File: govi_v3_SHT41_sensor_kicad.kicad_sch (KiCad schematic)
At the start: 5 parts

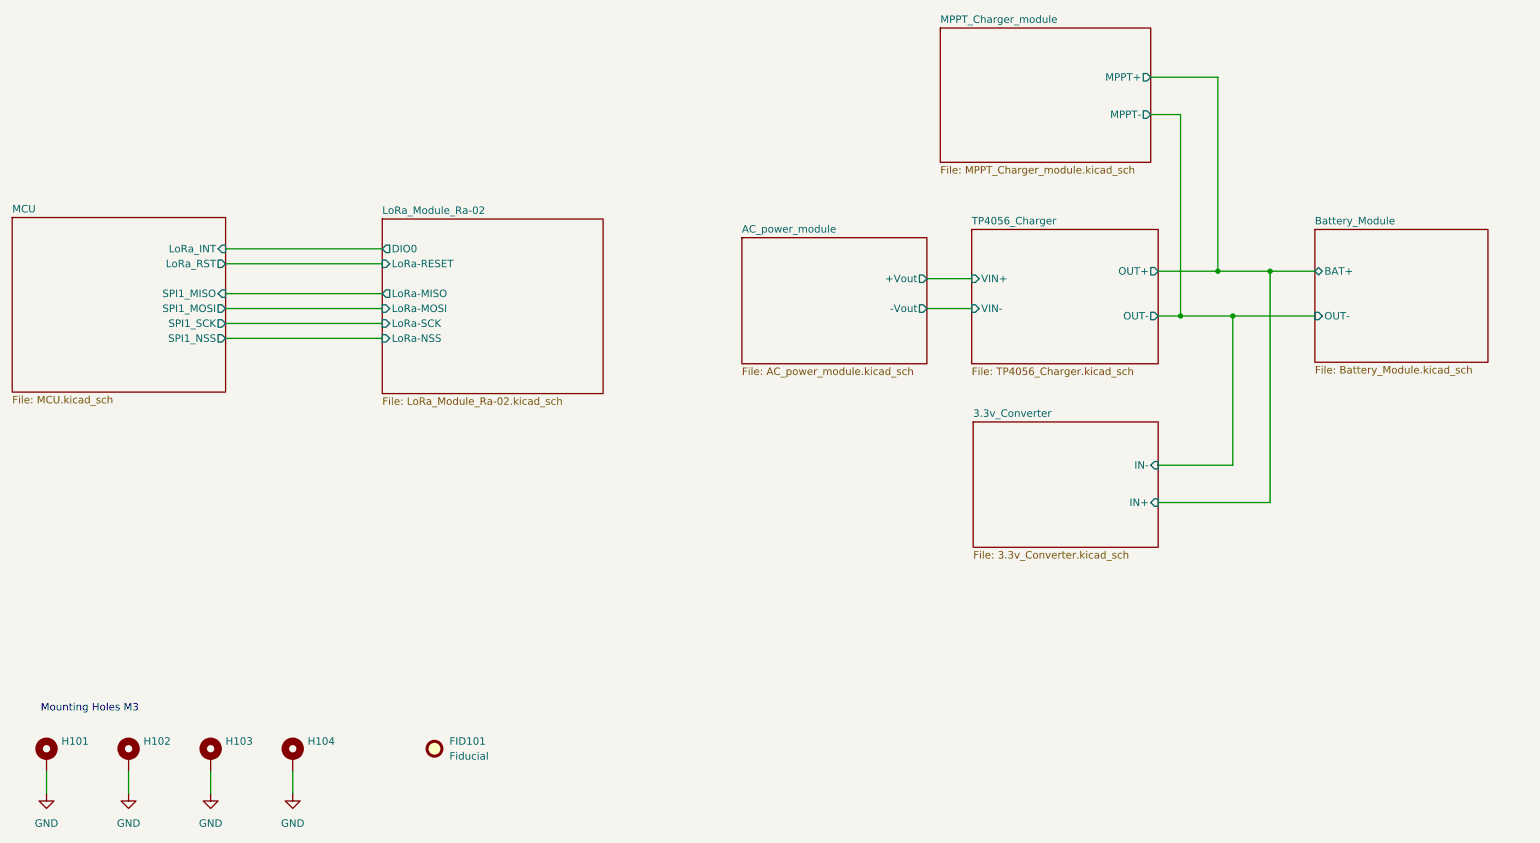
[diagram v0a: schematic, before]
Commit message: "Assign Footprints Done"
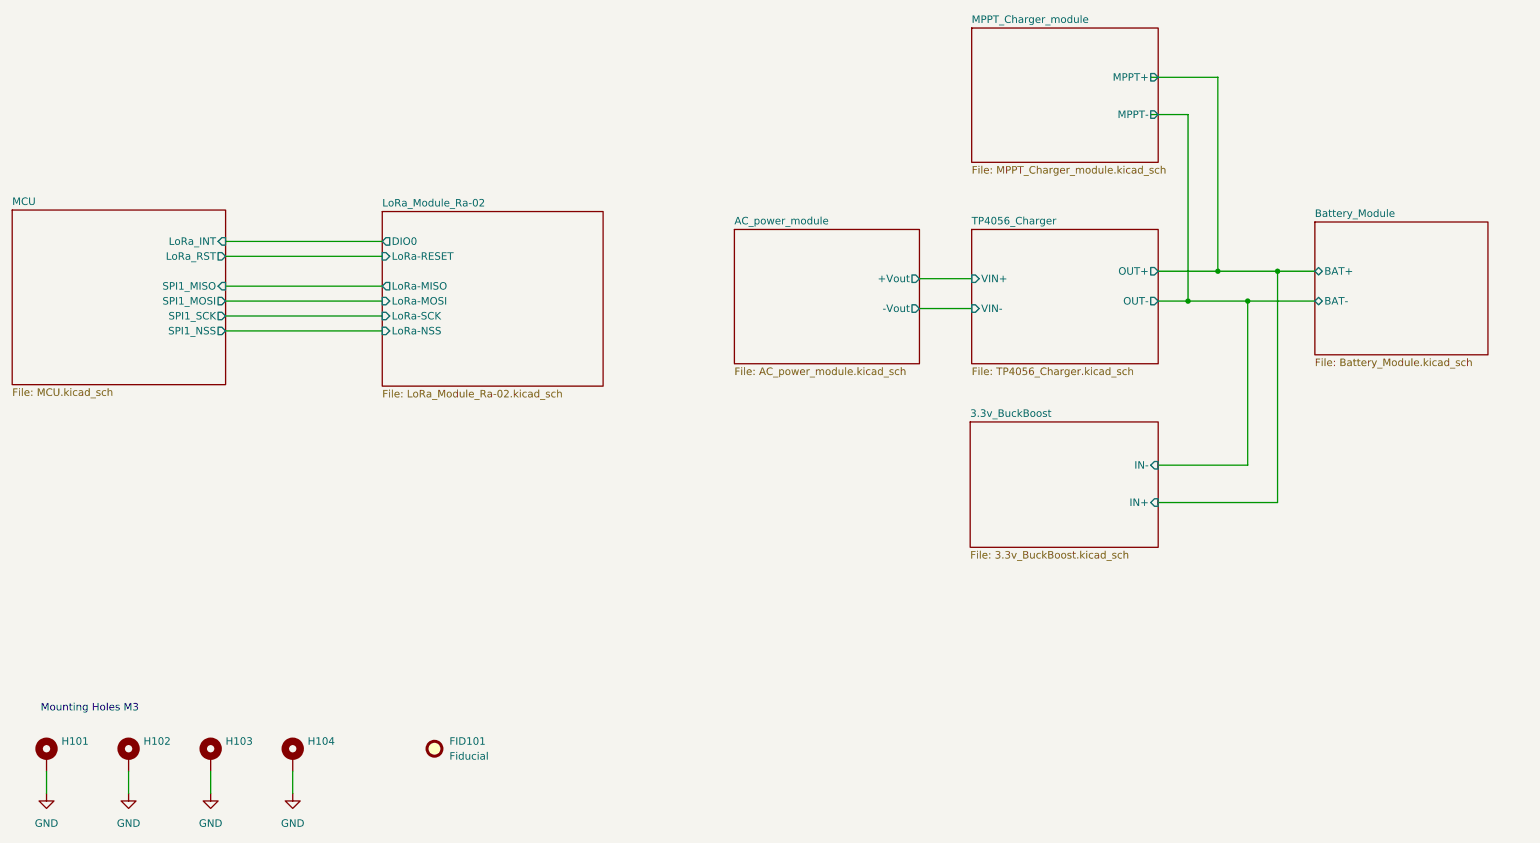
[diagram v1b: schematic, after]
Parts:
- FID101: footprint (none) -> Fiducial:Fiducial_1mm_Mask3mm
- H101, H102, H103, H104: footprint (none) -> MountingHole:MountingHole_3.2mm_M3_Pad_TopBottom
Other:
- sheet 3.3v_Converter renamed 3.3v_BuckBoost
- sheet 3.3v_BuckBoost: file 3.3v_Converter.kicad_sch -> 3.3v_BuckBoost.kicad_sch
- sheet Battery_Module ports: added BAT-; removed OUT-

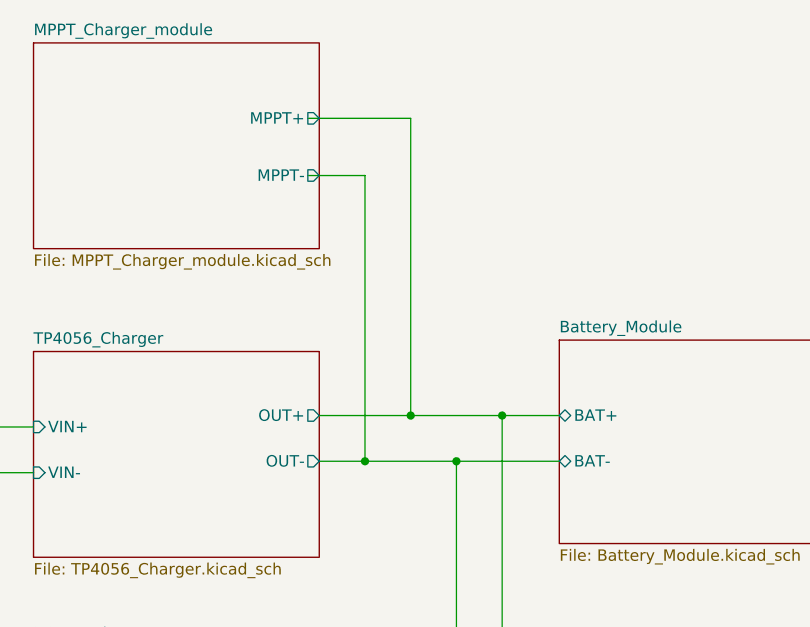
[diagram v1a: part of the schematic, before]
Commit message: "Some Component values were changed in MPPT sheet"
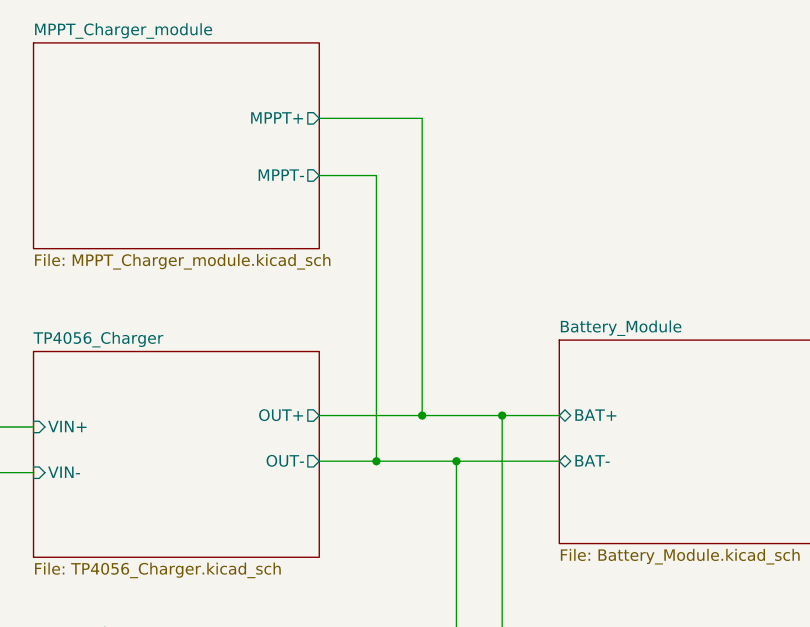
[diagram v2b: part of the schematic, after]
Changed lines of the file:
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@@
 	)
 	(junction
-		(at 224.79 90.17)
-		(diameter 0)
-		(color 0 0 0 0)
-	)
-	(junction
-		(at 229.87 85.09)
+		(at 226.06 90.17)
 		(diameter 0)
 		(color 0 0 0 0)
@@
 		(color 0 0 0 0)
 	)
+	(junction
+		(at 231.14 85.09)
+		(diameter 0)
+		(color 0 0 0 0)
+	)
 	(wire
 		(pts
@@
 	(wire
 		(pts
-			(xy 218.44 58.42) (xy 224.79 58.42)
+			(xy 219.71 58.42) (xy 226.06 58.42)
 		)
 		(stroke
@@
 	(wire
 		(pts
-			(xy 218.44 52.07) (xy 229.87 52.07)
-		)
-		(stroke
-			(width 0)
-			(type default)
-		)
-	)
-	(wire
-		(pts
-			(xy 219.71 85.09) (xy 229.87 85.09)
-		)
-		(stroke
-			(width 0)
-			(type default)
-		)
-	)
-	(wire
-		(pts
-			(xy 224.79 90.17) (xy 234.95 90.17)
+			(xy 219.71 52.07) (xy 231.14 52.07)
+		)
+		(stroke
+			(width 0)
+			(type default)
+		)
+	)
+	(wire
+		(pts
+			(xy 219.71 85.09) (xy 231.14 85.09)
 		)
 		(stroke
@@
 	(wire
 		(pts
-			(xy 229.87 85.09) (xy 229.87 52.07)
-		)
-		(stroke
-			(width 0)
-			(type default)
-		)
-	)
-	(wire
-		(pts
-			(xy 229.87 85.09) (xy 240.03 85.09)
+			(xy 231.14 85.09) (xy 231.14 52.07)
 		)
 		(stroke
@@
 	(wire
 		(pts
+			(xy 226.06 90.17) (xy 234.95 90.17)
+		)
+		(stroke
+			(width 0)
+			(type default)
+		)
+	)
+	(wire
+		(pts
 			(xy 30.48 170.18) (xy 30.48 173.99)
 		)
@@
 	(wire
 		(pts
-			(xy 224.79 58.42) (xy 224.79 90.17)
+			(xy 226.06 58.42) (xy 226.06 90.17)
 		)
 		(stroke
@@
 	(wire
 		(pts
-			(xy 219.71 90.17) (xy 224.79 90.17)
+			(xy 219.71 90.17) (xy 226.06 90.17)
 		)
 		(stroke
@@
 		)
 		(stroke
+			(width 0)
+			(type default)
+		)
+	)
+	(wire
+		(pts
+			(xy 231.14 85.09) (xy 240.03 85.09)
+		)
+		(stroke

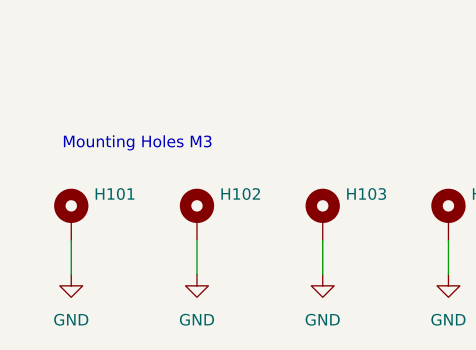
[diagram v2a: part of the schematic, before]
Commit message: "Before changing the orientation of the LoRa module. removing existing LoRa module routing."
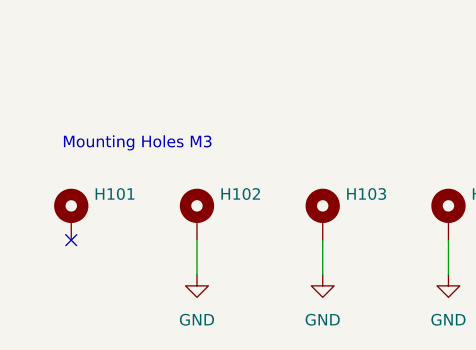
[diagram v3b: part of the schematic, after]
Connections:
- net GND: no longer H101.1
- no-connect marks 0 -> 1
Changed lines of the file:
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@@
 		(color 0 0 0 0)
 	)
+	(no_connect
+		(at 30.48 170.18)
+	)
 	(wire
 		(pts
@@
 		(pts
 			(xy 226.06 90.17) (xy 234.95 90.17)
-		)
-		(stroke
-			(width 0)
-			(type default)
-		)
-	)
-	(wire
-		(pts
-			(xy 30.48 170.18) (xy 30.48 173.99)
 		)
 		(stroke
@@
 					(unit 1)
 				)
-			)
-		)
-	)
-	(symbol
-		(lib_id "power:GND")
-		(at 30.48 173.99 0)
-		(unit 1)
-		(exclude_from_sim no)
-		(in_bom yes)
-		(on_board yes)
-		(dnp no)
-		(fields_autoplaced yes)
-		(property "Reference" "#PWR0101"
-			(at 30.48 180.34 0)
-			(effects
-				(font
-					(size 1.27 1.27)
-				)
-				(hide yes)
-			)
-		)
-		(property "Value" "GND"
-			(at 30.48 179.07 0)
-			(effects
-				(font
-					(size 1.27 1.27)
-				)
-			)
-		)
-		(property "Footprint" ""
-			(at 30.48 173.99 0)
-			(effects
-				(font
-					(size 1.27 1.27)
-				)
-				(hide yes)
-			)
-		)
-		(property "Datasheet" ""
-			(at 30.48 173.99 0)
-			(effects
-				(font
-					(size 1.27 1.27)
-				)
-				(hide yes)
-			)
-		)
-		(property "Description" "Power symbol creates a global label with name \"GND\" , ground"
-			(at 30.48 173.99 0)
-			(effects
-				(font
-					(size 1.27 1.27)
-				)
-				(hide yes)
-			)
-		)
-		(pin "1"
-		)
-		(instances
-			(project ""
-				(path "/ba95ddf4-72c6-4eeb-9c09-ae7c8e5af670"
-					(reference "#PWR0101")
-					(unit 1)
-				)
